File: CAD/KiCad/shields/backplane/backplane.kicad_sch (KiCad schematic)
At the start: 0 parts

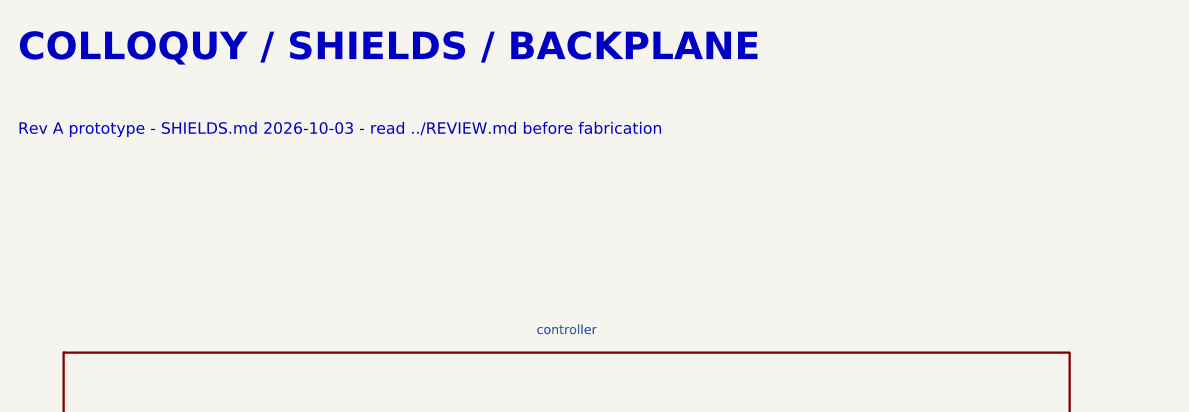
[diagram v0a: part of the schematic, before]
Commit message: Remove shield identification and adopt the simplified connector and Teensy pin maps
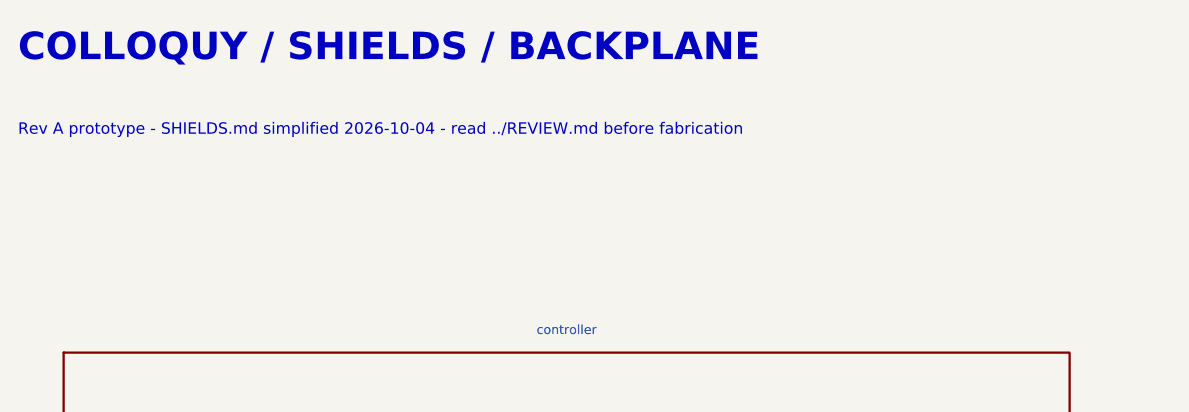
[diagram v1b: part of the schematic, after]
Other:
- note added: "Rev A prototype - SHIELDS.md simplified 2026-10-04 - read ../REVIEW.md before fabrication"
- note removed: "Rev A prototype - SHIELDS.md 2026-10-03 - read ../REVIEW.md before fabrication"

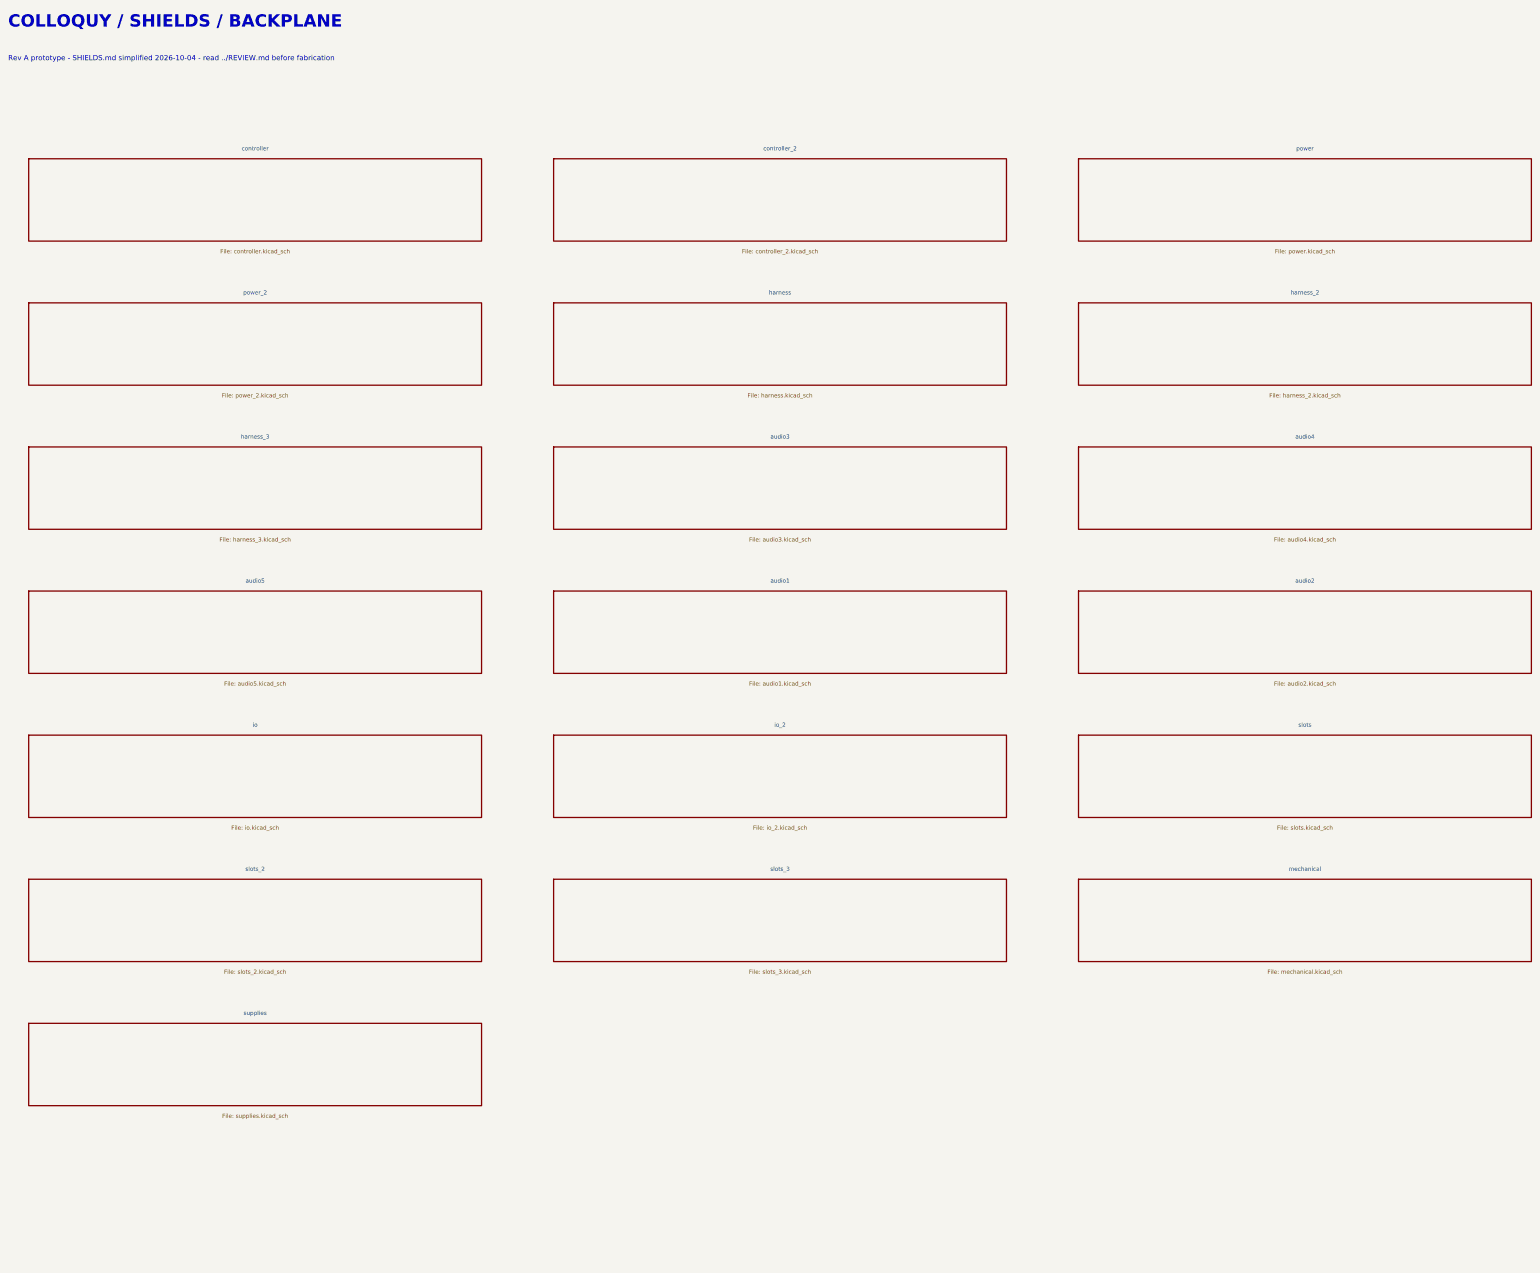
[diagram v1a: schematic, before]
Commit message: Route microphones directly to Teensy and remove the analyser buffer board
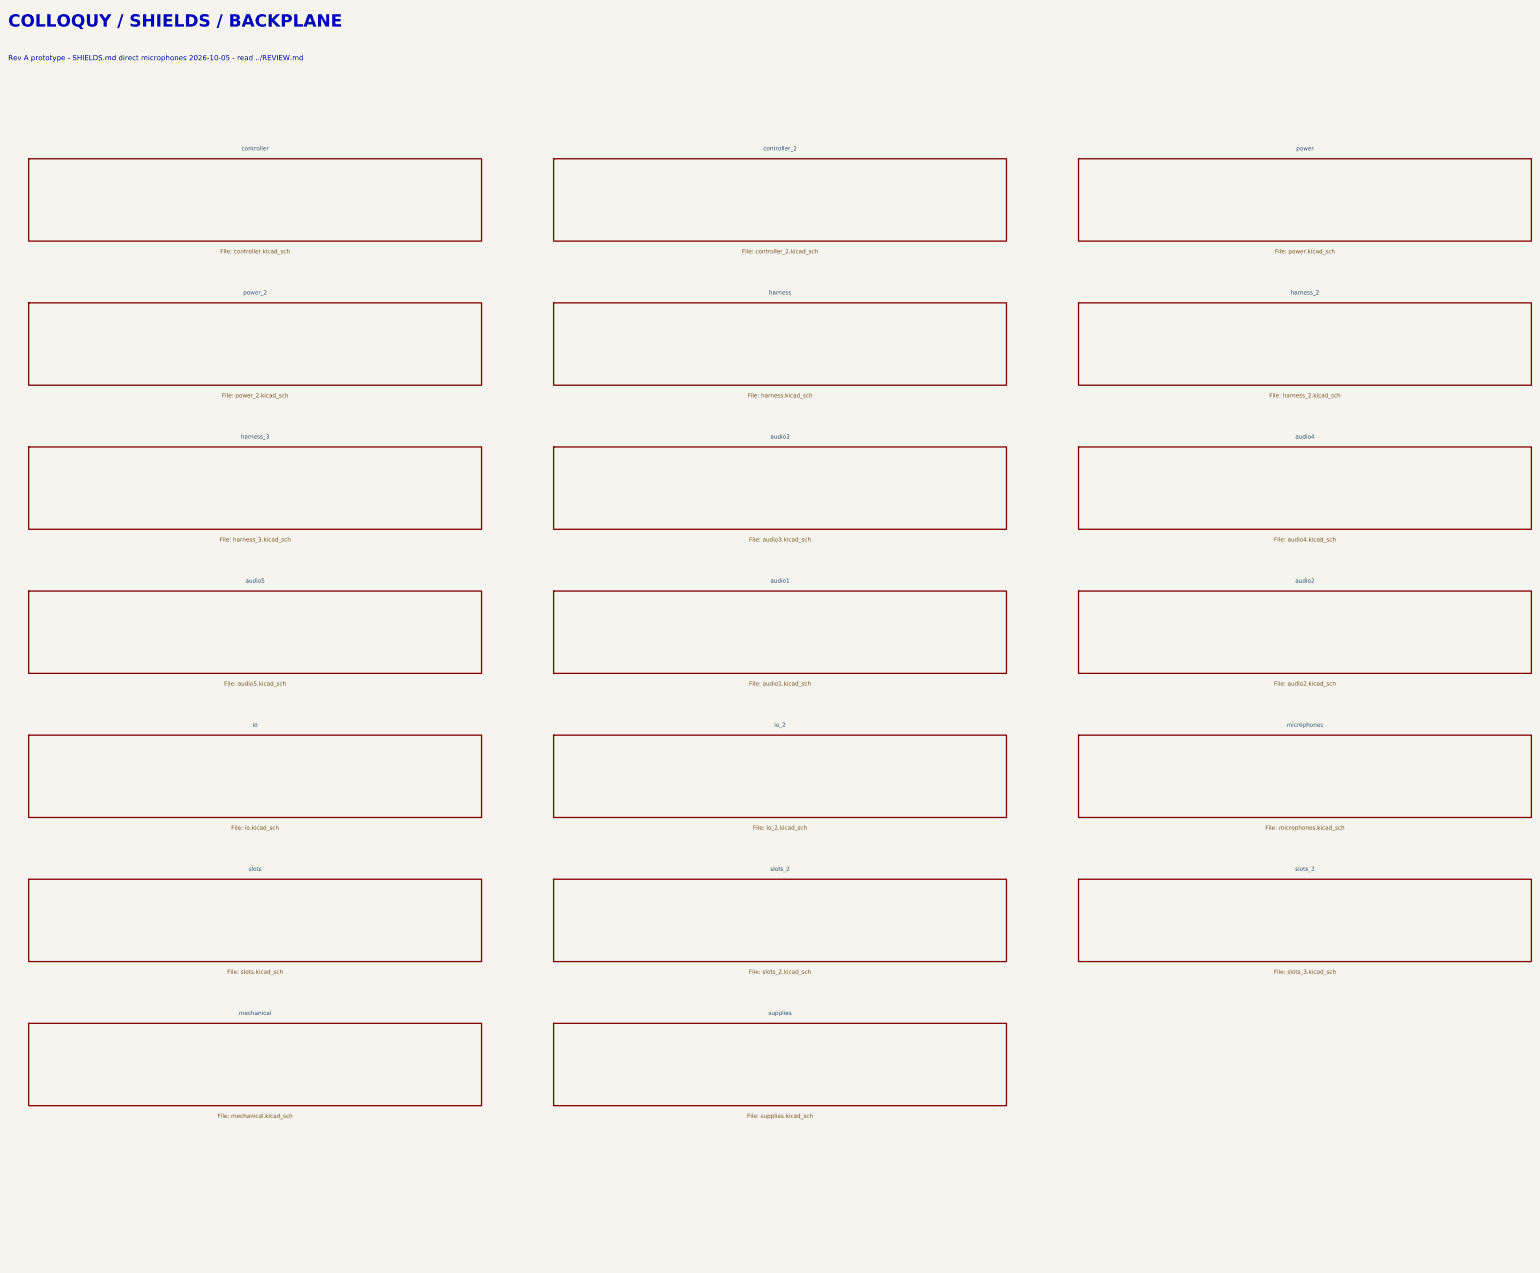
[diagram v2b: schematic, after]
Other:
- added sheet microphones (microphones.kicad_sch)
- note added: "Rev A prototype - SHIELDS.md direct microphones 2026-10-05 - read ../REVIEW.md"
- note removed: "Rev A prototype - SHIELDS.md simplified 2026-10-04 - read ../REVIEW.md before fabrication"

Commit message: Update shields for Thomas RC cards, debug headers and body microphones
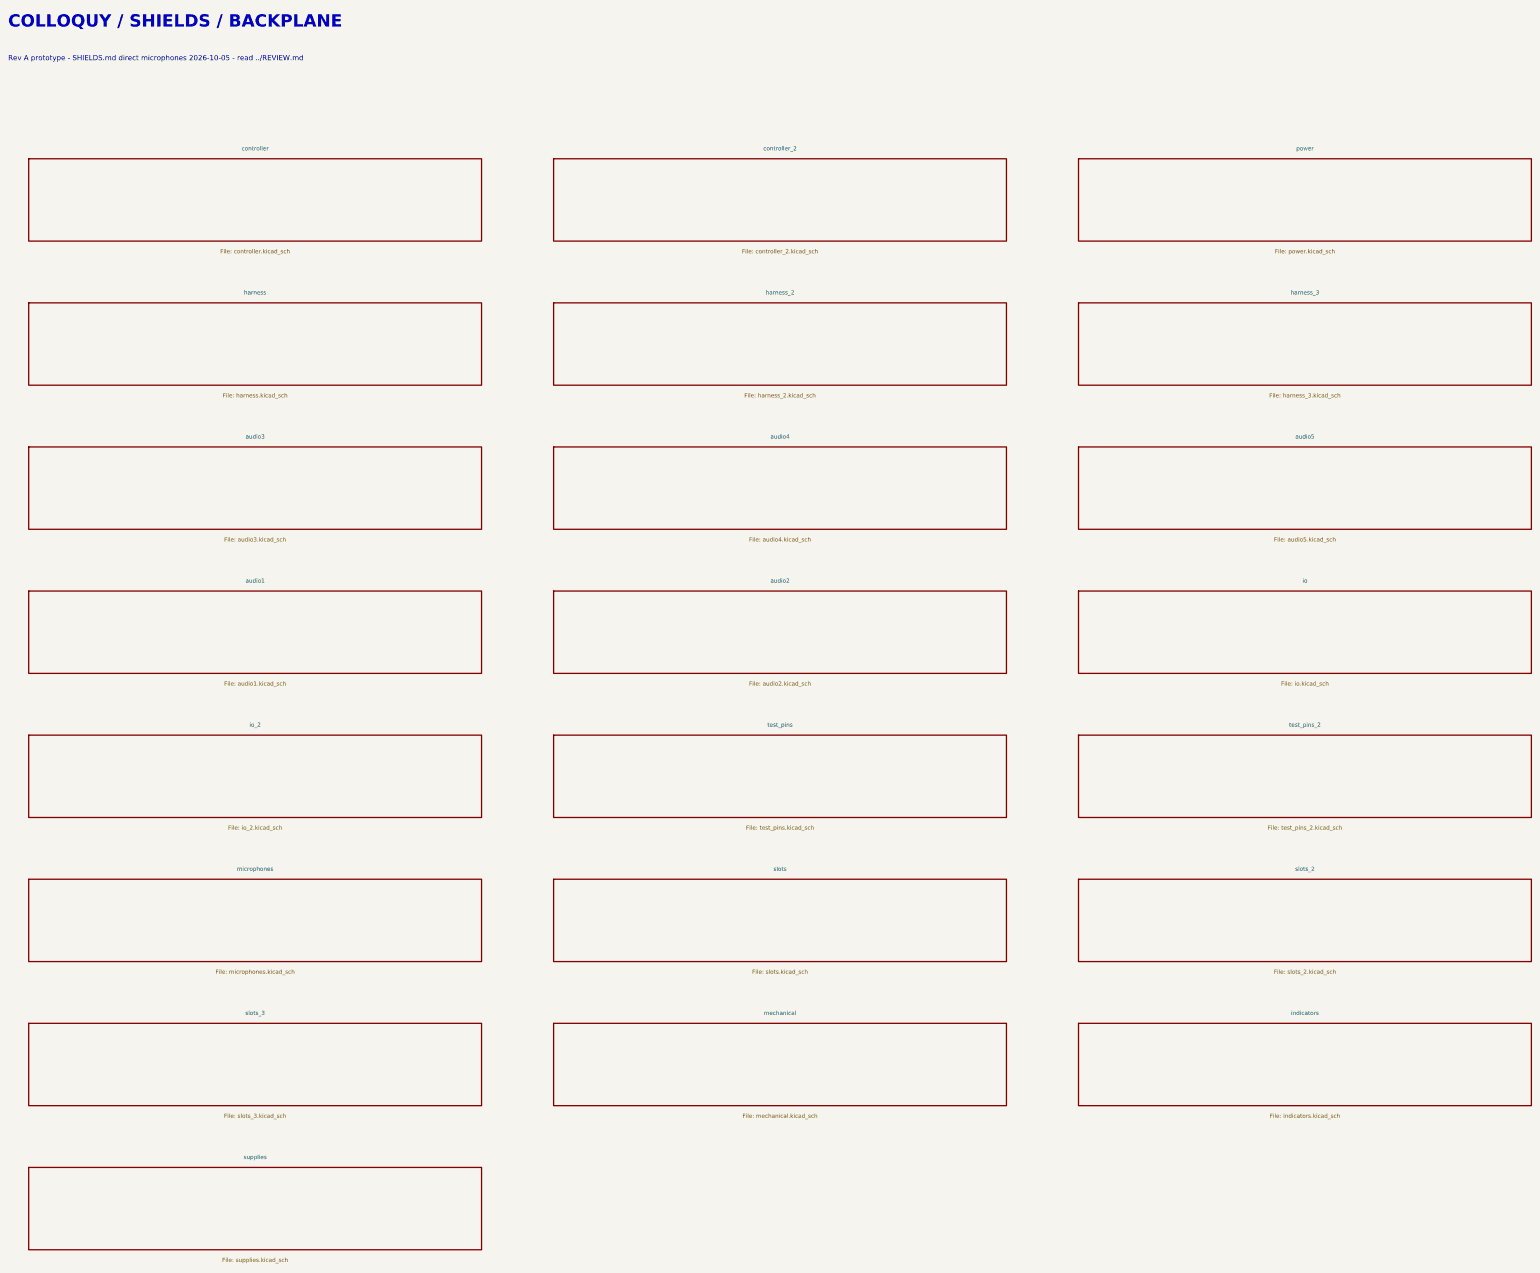
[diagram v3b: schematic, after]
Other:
- removed sheet power_2
- added sheet indicators (indicators.kicad_sch)
- added sheet test_pins (test_pins.kicad_sch)
- added sheet test_pins_2 (test_pins_2.kicad_sch)
